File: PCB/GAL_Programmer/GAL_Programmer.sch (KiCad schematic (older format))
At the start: 9 parts, among them P1 Power, P2 Analog, P3 Digital, P4 Digital, P5 CONN_01X01, P6 CONN_01X01, P7 CONN_01X01, P8 CONN_01X01

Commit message: Conexion de ATF22V10 y  ATF16V8 en el mismo socket
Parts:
- removed U?: GAL16V8, symbol Logic_Programmable:GAL16V8
- added R? (x9): 4k7, symbol Device:R_Small_US
- added U?: ATF16V8, symbol Logic_Devices:ATF16V8
- added U?: ATF22V10, symbol Logic_Devices:ATF22V10
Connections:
- net labels added: EDIT, PV, RA0, RA1, RA2, RA3, RA4, RA5, SCL, SDI, SDO, STR
- wire segments 38 -> 145

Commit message: Se termino el esquematico, falta hacer una revisión a detalle de las conexiones y resistencias que se deben usar, falta agregar capacitores al diseño. Se generó el netlist y se empezo el diseño del PCB
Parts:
- added R10: 4k7, Resistor_THT:R_Axial_DIN0207_L6.3mm_D2.5mm_P7.62mm_Horizontal, symbol Device:R_Small_US
- added U3: MT3608, Socket_Arduino_Uno:MT3608_Module, symbol DC_DC:MT3608
- R1, R2, R3, R4, R5, R6, R7, R8, R9: renamed from R?; footprint (none) -> Resistor_THT:R_Axial_DIN0207_L6.3mm_D2.5mm_P7.62mm_Horizontal
- U1: renamed from U?; footprint (none) -> Package_DIP:DIP-20_W7.62mm_Socket_LongPads
- U2: renamed from U?; footprint (none) -> Package_DIP:DIP-24_W7.62mm_Socket_LongPads
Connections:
- net labels added: 11(MOSI), VPP
- net labels removed: +3.3V, 11(**/MOSI)
- wire segments 145 -> 153
- no-connect marks 5 -> 16
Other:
- note added: "4.7 kΩ x 5"
- note added: "Conexion con pines de Arduino"
- note added: "FUENTE DC/DC STEP UP"

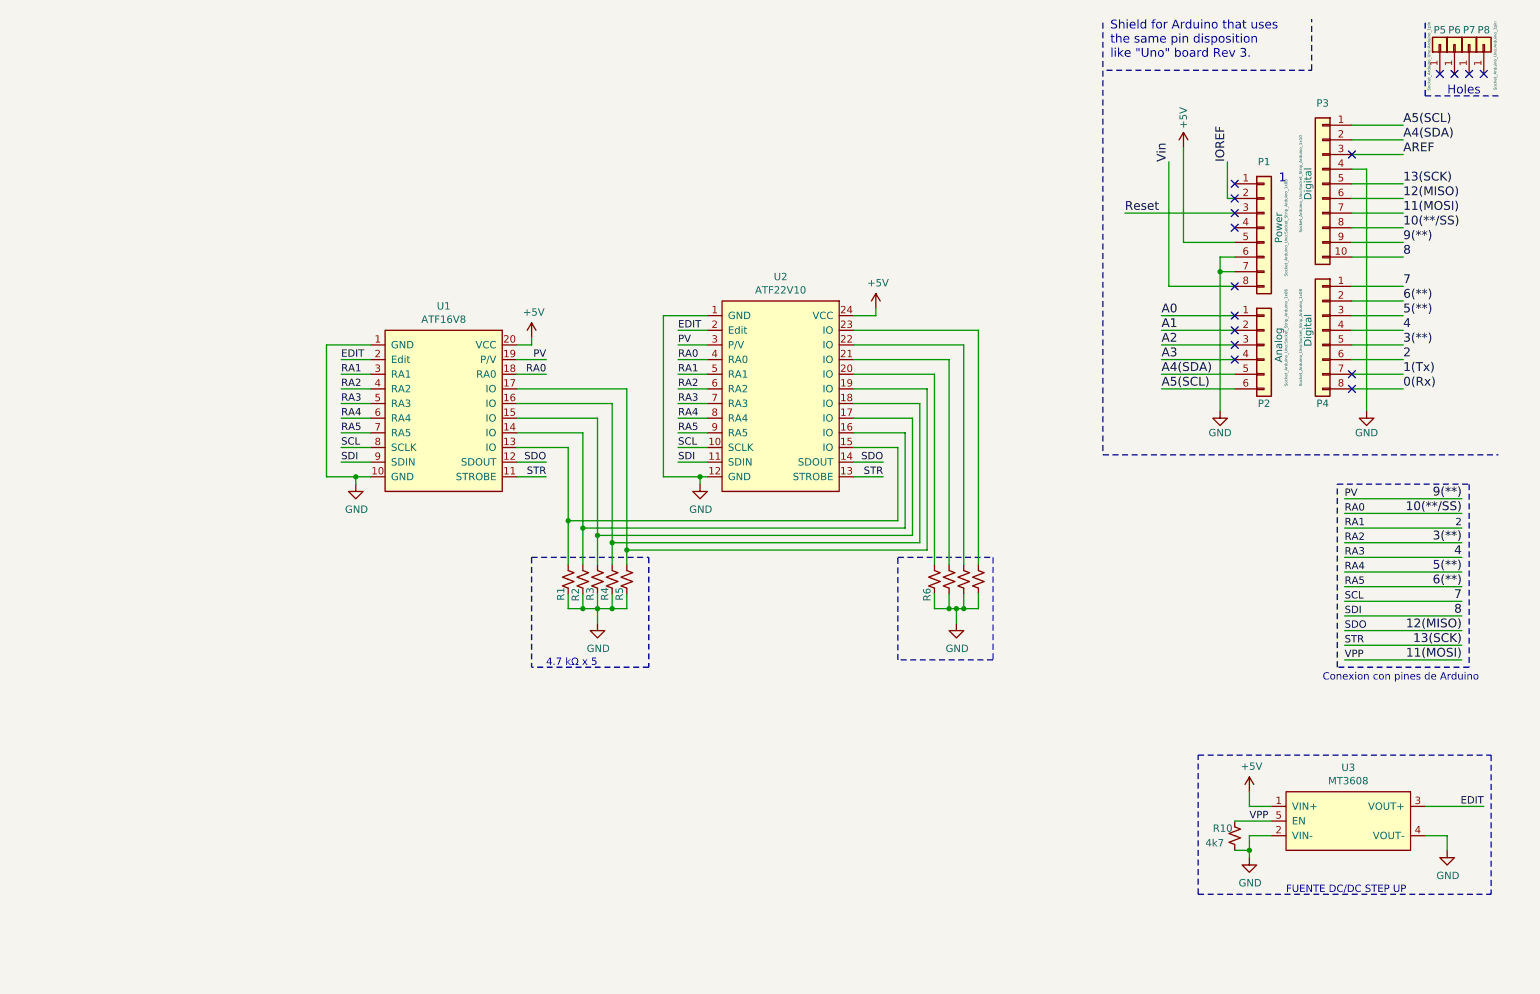
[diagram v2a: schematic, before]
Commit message: Se agregaron capacitores al esquematico y al PCB, esta por empezar el ruteo del PCB
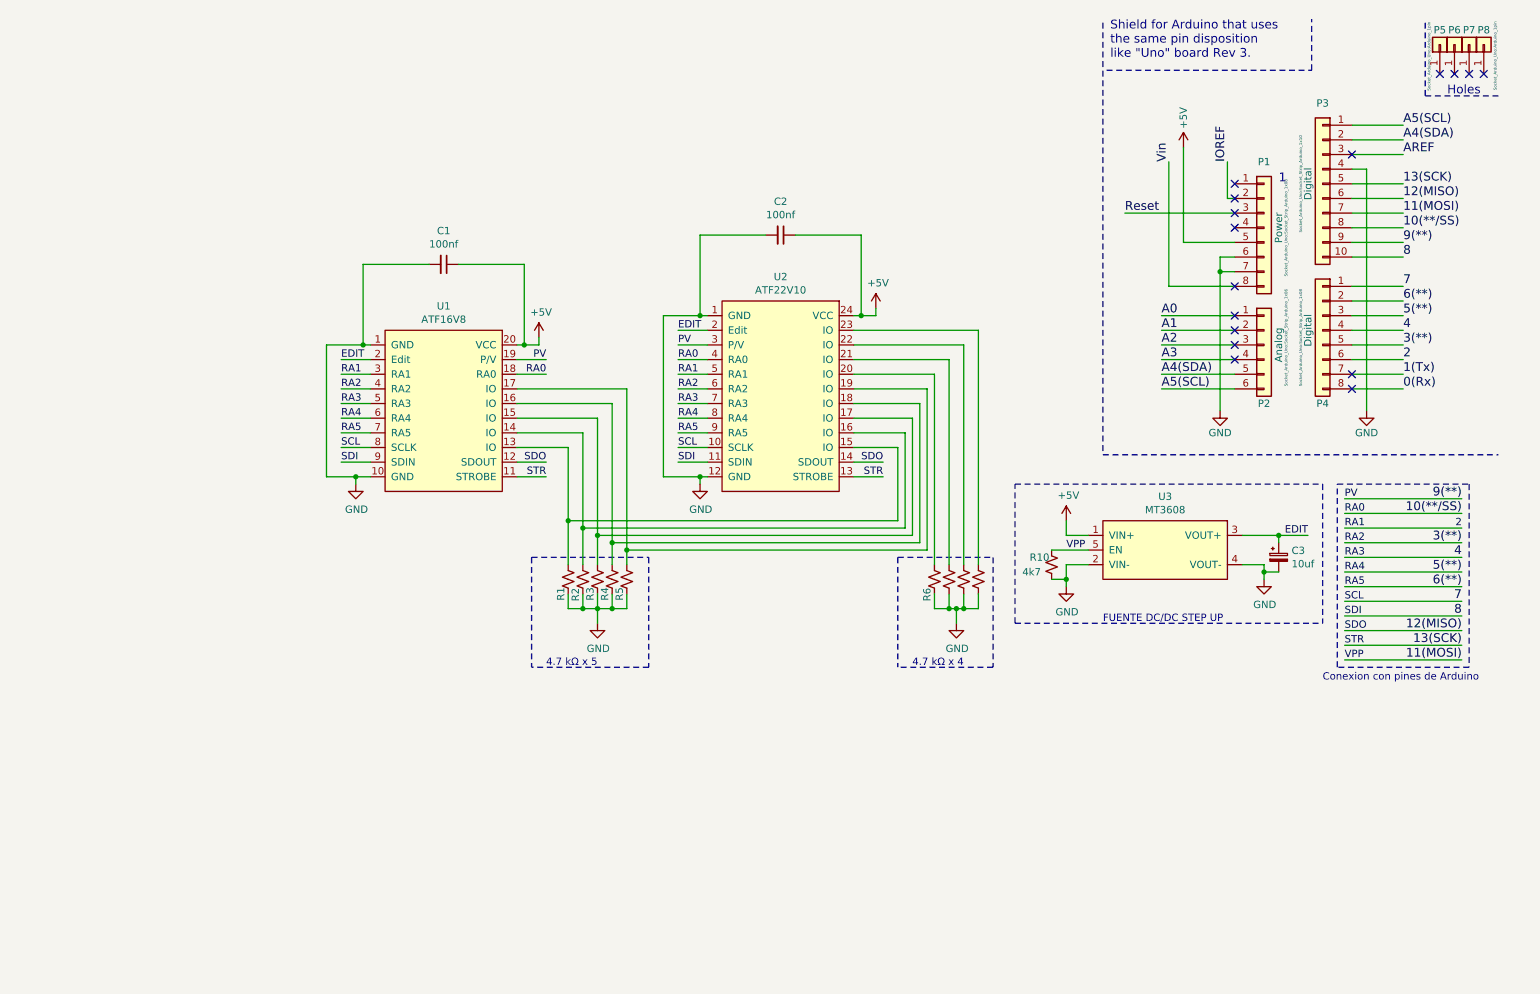
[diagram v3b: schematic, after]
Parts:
- added C1, C2: 100nf, Capacitor_THT:C_Disc_D5.0mm_W2.5mm_P2.50mm, symbol Device:C_Small
- added C3: 10uf, Capacitor_THT:C_Radial_D5.0mm_H7.0mm_P2.00mm, symbol Device:CP_Small
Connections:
- net +5V: now also C1.1, C2.1
- net EDIT: now also C3.1
- net GND: now also C1.2, C2.2, C3.2
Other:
- note added: "4.7 kΩ x 4"
- moved on the sheet: R10, U3
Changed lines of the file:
@@
 	6950 2450 6950 2500
 Wire Wire Line
-	6950 2500 6800 2500
+	6950 2500 6850 2500
 $Comp
 L power:GND #PWR08
@@
 	5750 3600 5800 3600
 Wire Wire Line
-	5500 2500 5800 2500
+	5500 2500 5750 2500
 Wire Wire Line
 	5500 3600 5750 3600
@@
 	3400 3600 3500 3600
 Wire Wire Line
-	3500 2700 3200 2700
+	3500 2700 3450 2700
 Wire Wire Line
 	3200 2700 3200 3600
@@
 	3200 3600 3400 3600
 Connection ~ 3400 3600
-Wire Wire Line
-	4600 2650 4600 2700
-Wire Wire Line
-	4600 2700 4500 2700
 Wire Wire Line
 	6800 3400 7100 3400
@@
 	4600 4150 5400 4150
 Wire Notes Line
-	5400 4900 4600 4900
-Wire Notes Line
 	7100 4150 7750 4150
 Wire Notes Line
-	7750 4150 7750 4850
-Wire Notes Line
-	7750 4850 7100 4850
-Wire Notes Line
-	7100 4850 7100 4150
+	7750 4900 7100 4900
 Text Label 5600 2600 0    50   ~ 0
 EDIT
@@
 Wire Wire Line
 	10150 4850 10950 4850
-$Comp
-L DC_DC:MT3608 U3
-U 1 1 61971C71
-P 10150 5950
-F 0 "U3" H 10175 6315 50  0000 C CNN
-F 1 "MT3608" H 10175 6224 50  0000 C CNN
-F 2 "Socket_Arduino_Uno:MT3608_Module" H 10150 5950 50  0001 C CNN
-F 3 "" H 10150 5950 50  0001 C CNN
-	1    10150 5950
-	1    0    0    -1
-$EndComp
-Wire Wire Line
-	9500 5750 9500 5850
-Wire Wire Line
-	9500 5850 9650 5850
-$Comp
-L power:GND #PWR012
-U 1 1 6197BA10
-P 9500 6200
-F 0 "#PWR012" H 9500 5950 50  0001 C CNN
-F 1 "GND" H 9505 6027 50  0000 C CNN
-F 2 "" H 9500 6200 50  0001 C CNN
-F 3 "" H 9500 6200 50  0001 C CNN
-	1    9500 6200
-	1    0    0    -1
-$EndComp
-Wire Wire Line
-	9500 6200 9500 6150
-Wire Wire Line
-	9500 6050 9650 6050
-Text Label 9500 5950 0    50   ~ 0
-VPP
-$Comp
-L power:GND #PWR014
-U 1 1 6199444D
-P 10850 6150
-F 0 "#PWR014" H 10850 5900 50  0001 C CNN
-F 1 "GND" H 10855 5977 50  0000 C CNN
-F 2 "" H 10850 6150 50  0001 C CNN
-F 3 "" H 10850 6150 50  0001 C CNN
-	1    10850 6150
-	1    0    0    -1
-$EndComp
-Wire Wire Line
-	10850 6150 10850 6050
-Wire Wire Line
-	10850 6050 10700 6050
-Wire Notes Line
-	11150 5500 11150 6450
-Wire Notes Line
-	9150 6450 9150 5500
-Text Notes 9750 6450 0    50   ~ 0
-FUENTE DC/DC STEP UP
-Text Label 11100 5850 2    50   ~ 0
-EDIT
-Text Notes 5050 4900 2    50   ~ 0
-4.7 kΩ x 5
 Wire Notes Line
 	5400 4150 5400 4900
-Wire Notes Line
-	4600 4150 4600 4900
-$Comp
-L Device:R_Small_US R10
-U 1 1 61A09D73
-P 9400 6050
-F 0 "R10" H 9250 6100 50  0000 L CNN
-F 1 "4k7" H 9200 6000 50  0000 L CNN
-F 2 "Resistor_THT:R_Axial_DIN0207_L6.3mm_D2.5mm_P7.62mm_Horizontal" H 9400 6050 50  0001 C CNN
-F 3 "~" H 9400 6050 50  0001 C CNN
-	1    9400 6050
-	1    0    0    -1
-$EndComp
-Wire Wire Line
-	9400 5950 9650 5950
-Wire Wire Line
-	9400 6150 9500 6150
-Connection ~ 9500 6150
-Wire Wire Line
-	9500 6150 9500 6050
-Wire Notes Line
-	9150 6450 11150 6450
-Wire Notes Line
-	9150 5500 11150 5500
 NoConn ~ 9400 2500
 NoConn ~ 9400 2600
@@
 L power:+5V #PWR06
 U 1 1 618FA16A
-P 4600 2650
-F 0 "#PWR06" H 4600 2500 50  0001 C CNN
-F 1 "+5V" H 4615 2823 50  0000 C CNN
-F 2 "" H 4600 2650 50  0001 C CNN
-F 3 "" H 4600 2650 50  0001 C CNN
-	1    4600 2650
-	1    0    0    -1
-$EndComp
-$Comp
-L power:+5V #PWR011
-U 1 1 6197354D
-P 9500 5750
-F 0 "#PWR011" H 9500 5600 50  0001 C CNN
-F 1 "+5V" H 9515 5923 50  0000 C CNN
-F 2 "" H 9500 5750 50  0001 C CNN
-F 3 "" H 9500 5750 50  0001 C CNN
-	1    9500 5750
+P 4650 2650
+F 0 "#PWR06" H 4650 2500 50  0001 C CNN
+F 1 "+5V" H 4665 2823 50  0000 C CNN
+F 2 "" H 4650 2650 50  0001 C CNN
+F 3 "" H 4650 2650 50  0001 C CNN
+	1    4650 2650
 	1    0    0    -1
 $EndComp
@@
 	1    0    0    -1
 $EndComp
-Wire Wire Line
-	10700 5850 11100 5850
 NoConn ~ 10200 1400
 NoConn ~ 10200 3000
 NoConn ~ 10200 2900
 NoConn ~ 9400 1900
+$Comp
+L Device:C_Small C2
+U 1 1 618FBA00
+P 6300 1950
+F 0 "C2" V 6071 1950 50  0000 C CNN
+F 1 "100nf" V 6162 1950 50  0000 C CNN
+F 2 "Capacitor_THT:C_Disc_D5.0mm_W2.5mm_P2.50mm" H 6300 1950 50  0001 C CNN
+F 3 "~" H 6300 1950 50  0001 C CNN
+	1    6300 1950
+	0    1    1    0
+$EndComp
+Wire Wire Line
+	6400 1950 6850 1950
+Wire Wire Line
+	6850 1950 6850 2500
+Connection ~ 6850 2500
+Wire Wire Line
+	6850 2500 6800 2500
+Wire Wire Line
+	6200 1950 5750 1950
+Wire Wire Line
+	5750 1950 5750 2500
+Connection ~ 5750 2500
+Wire Wire Line
+	5750 2500 5800 2500
+Wire Wire Line
+	4100 2150 4550 2150
+Wire Wire Line
+	3900 2150 3450 2150
+$Comp
+L Device:C_Small C1
+U 1 1 6190DCB8
+P 4000 2150
+F 0 "C1" V 3771 2150 50  0000 C CNN
+F 1 "100nf" V 3862 2150 50  0000 C CNN
+F 2 "Capacitor_THT:C_Disc_D5.0mm_W2.5mm_P2.50mm" H 4000 2150 50  0001 C CNN
+F 3 "~" H 4000 2150 50  0001 C CNN
+	1    4000 2150
+	0    1    1    0
+$EndComp
+Wire Wire Line
+	3450 2150 3450 2700
+Connection ~ 3450 2700
+Wire Wire Line
+	3450 2700 3200 2700
+Wire Wire Line
+	4550 2150 4550 2700
+Connection ~ 4550 2700
+Wire Wire Line
+	4550 2700 4500 2700
+Wire Wire Line
+	4650 2700 4650 2650
+Wire Wire Line
+	4550 2700 4650 2700
+Wire Notes Line
+	4600 4150 4600 4900
+Text Notes 5050 4900 2    50   ~ 0
+4.7 kΩ x 5
+Wire Notes Line
+	5400 4900 4600 4900
+Text Notes 7550 4900 2    50   ~ 0
+4.7 kΩ x 4
+Wire Notes Line
+	7100 4150 7100 4900
+Wire Notes Line
+	7750 4150 7750 4900
+Wire Wire Line
+	9600 4250 9600 4200
+Connection ~ 9600 4250
+Wire Wire Line
+	9700 4250 9600 4250
+Wire Wire Line
+	9700 4000 9900 4000
+Connection ~ 9700 4000
+Wire Wire Line
+	9700 4050 9700 4000
+$Comp
+L Device:CP_Small C3
+U 1 1 618E1C44
+P 9700 4150
+F 0 "C3" H 9788 4196 50  0000 L CNN
+F 1 "10uf" H 9788 4105 50  0000 L CNN
+F 2 "Capacitor_THT:C_Radial_D5.0mm_H7.0mm_P2.00mm" H 9700 4150 50  0001 C CNN
+F 3 "~" H 9700 4150 50  0001 C CNN
+	1    9700 4150
+	1    0    0    -1
+$EndComp
+Wire Wire Line
+	9450 4000 9700 4000
+$Comp
+L power:+5V #PWR011
+U 1 1 6197354D
+P 8250 3900
+F 0 "#PWR011" H 8250 3750 50  0001 C CNN
+F 1 "+5V" H 8265 4073 50  0000 C CNN
+F 2 "" H 8250 3900 50  0001 C CNN
+F 3 "" H 8250 3900 50  0001 C CNN
+	1    8250 3900
+	1    0    0    -1
+$EndComp
+Wire Wire Line
+	8250 4300 8250 4200
+Connection ~ 8250 4300
+Wire Wire Line
+	8150 4300 8250 4300
+Wire Wire Line
+	8150 4100 8400 4100
+$Comp
+L Device:R_Small_US R10
+U 1 1 61A09D73
+P 8150 4200
+F 0 "R10" H 8000 4250 50  0000 L CNN
+F 1 "4k7" H 7950 4150 50  0000 L CNN
+F 2 "Resistor_THT:R_Axial_DIN0207_L6.3mm_D2.5mm_P7.62mm_Horizontal" H 8150 4200 50  0001 C CNN
+F 3 "~" H 8150 4200 50  0001 C CNN
+	1    8150 4200
+	1    0    0    -1
+$EndComp
+Text Label 9900 4000 2    50   ~ 0
+EDIT
+Text Notes 8500 4600 0    50   ~ 0
+FUENTE DC/DC STEP UP
+Wire Notes Line
+	7900 4600 7900 3650
+Wire Notes Line
+	10000 3650 10000 4600
+Wire Wire Line
+	9600 4200 9450 4200
+Wire Wire Line
+	9600 4300 9600 4250
+$Comp
+L power:GND #PWR014
+U 1 1 6199444D
+P 9600 4300
+F 0 "#PWR014" H 9600 4050 50  0001 C CNN
+F 1 "GND" H 9605 4127 50  0000 C CNN
+F 2 "" H 9600 4300 50  0001 C CNN
+F 3 "" H 9600 4300 50  0001 C CNN
+	1    9600 4300
+	1    0    0    -1
+$EndComp
+Text Label 8250 4100 0    50   ~ 0
+VPP
+Wire Wire Line
+	8250 4200 8400 4200
+Wire Wire Line
+	8250 4350 8250 4300
+$Comp
+L power:GND #PWR012
+U 1 1 6197BA10
+P 8250 4350
+F 0 "#PWR012" H 8250 4100 50  0001 C CNN
+F 1 "GND" H 8255 4177 50  0000 C CNN
+F 2 "" H 8250 4350 50  0001 C CNN
+F 3 "" H 8250 4350 50  0001 C CNN
+	1    8250 4350
+	1    0    0    -1
+$EndComp
+Wire Wire Line
+	8250 4000 8400 4000
+Wire Wire Line
+	8250 3900 8250 4000
+$Comp
+L DC_DC:MT3608 U3
+U 1 1 61971C71
+P 8900 4100
+F 0 "U3" H 8925 4465 50  0000 C CNN
+F 1 "MT3608" H 8925 4374 50  0000 C CNN
+F 2 "Socket_Arduino_Uno:MT3608_Module" H 8900 4100 50  0001 C CNN
+F 3 "" H 8900 4100 50  0001 C CNN
+	1    8900 4100
+	1    0    0    -1
+$EndComp
+Wire Notes Line
+	7900 3650 10000 3650
+Wire Notes Line
+	7900 4600 10000 4600
 $EndSCHEMATC

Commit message: Interfaz: Se terminaron los background workers, todos fueron probados y funcionaron correctamente, se creo el empaquetado del instalador, falta probar con alguien mas para liberar el primer versión, se hicieron cambios de estetica, en colores de botones, se agrego la función al momento de presionar el boton de DESCONECTAR, se reinicien los colores de todos los botones y el progress bar. La interfaz esta lista y funcional. Programa el GAL16V8 sin problemas, el 22V10 tiene problemas que no lo detecta como tal pero si funciona la programación. Se agregaron iconos de circuitos intergados a la interfaz
PCB: Se termino el listado de componentes, el ruteado y se pudo agregar el socket ZIF para 20 y 24 pines, todo el ruteado se completo sin problemas y en orden, se tuvo que agrandar el PCB ya que la fuente CD/CD no cabia por el tamaño de los socket ZIF. Falta agregar información de la construcción y detalles esteticos. Queda pendiente probar con Arduino Leonardo y hacer una prueba de funcionamiento, esto serviría para los programadores como standalone que podrían usarse fijamente.
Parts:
- added J1: Conn_01x02_Male, Connector_PinHeader_2.54mm:PinHeader_1x02_P2.54mm_Vertical, symbol Connector:Conn_01x02_Male
- added U4: ATF16V8, Socket:DIP_Socket-20_W4.3_W5.08_W7.62_W10.16_W10.9_3M_220-3342-00-0602J, symbol Logic_Devices:ATF16V8
- added U5: ATF22V10, Socket:DIP_Socket-24_W11.9_W12.7_W15.24_W17.78_W18.5_3M_224-1275-00-0602J, symbol Logic_Devices:ATF22V10
- C3: symbol Device:CP_Small -> GAL_Programmer-rescue:CP_Small-Device
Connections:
- net +5V: now also U4.20 (VCC), U5.24 (VCC)
- net 10(**/SS): now also U4.18 (RA0), U5.4 (RA0)
- net 12(MISO): now also U4.12 (SDOUT), U5.14 (SDOUT)
- net 13(SCK): now also U4.11 (STROBE), U5.13 (STROBE)
- net 2: now also U4.3 (RA1), U5.5 (RA1)
- net 3(**): now also U4.4 (RA2), U5.6 (RA2)
- net 4: now also U4.5 (RA3), U5.7 (RA3)
- net 5(**): now also U4.6 (RA4), U5.8 (RA4)
- net 6(**): now also U4.7 (RA5), U5.9 (RA5)
- net 7: now also U4.8 (SCLK), U5.10 (SCLK)
- net 8: now also U4.9 (SDIN), U5.11 (SDIN)
- net 9(**): now also U4.19 (P/V), U5.3 (P/V)
- net EDIT: now also J1.1 (Pin_1), U4.2 (Edit), U5.2 (Edit); no longer C3.1, U3.3 (VOUT+)
- net GND: now also U4.1 (GND), U4.10 (GND), U5.1 (GND), U5.12 (GND)
- net R1: now reaches R1.1, U1.13 (IO), U2.15 (IO)
- net R1: now also U4.13 (IO), U5.15 (IO)
- net R2: now reaches R2.1, U1.14 (IO), U2.16 (IO)
- net R2: now also U4.14 (IO), U5.16 (IO)
- net R3: now reaches R3.1, U1.15 (IO), U2.17 (IO)
- net R3: now also U4.15 (IO), U5.17 (IO)
- net R4: now reaches R4.1, U1.16 (IO), U2.18 (IO)
- net R4: now also U4.16 (IO), U5.18 (IO)
- net R5: now reaches R5.1, U1.17 (IO), U2.19 (IO)
- net R5: now also U4.17 (IO), U5.19 (IO)
- net R6: now reaches R6.1, U2.20 (IO)
- net R6: now also U5.20 (IO)
- net R7: now reaches R7.1, U2.21 (IO)
- net R7: now also U5.21 (IO)
- net R8: now reaches R8.1, U2.22 (IO)
- net R8: now also U5.22 (IO)
- net R9: now reaches R9.1, U2.23 (IO)
- net R9: now also U5.23 (IO)
- net A4(SDA): no longer names the net of P2.5 (Pin_5)
- net A4(SDA): no longer P3.2 (Pin_2)
- net A5(SCL): no longer names the net of P2.6 (Pin_6)
- net A5(SCL): no longer P3.1 (Pin_1)
- new net: C3.1, J1.2 (Pin_2), U3.3 (VOUT+)
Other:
- note added: "Socket para base ZIF de CI"
- note added: "Socket para base sencilla de CI"
- moved on the sheet: C1, C2, C3, R1, R10, R2, R3, R4, R5, R6, U1, U2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
